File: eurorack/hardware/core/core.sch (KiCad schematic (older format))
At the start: 3 parts, among them U1 STM32F427VGT6, U2 TLV320AIC23BPW, U3 LM1117F-3.3

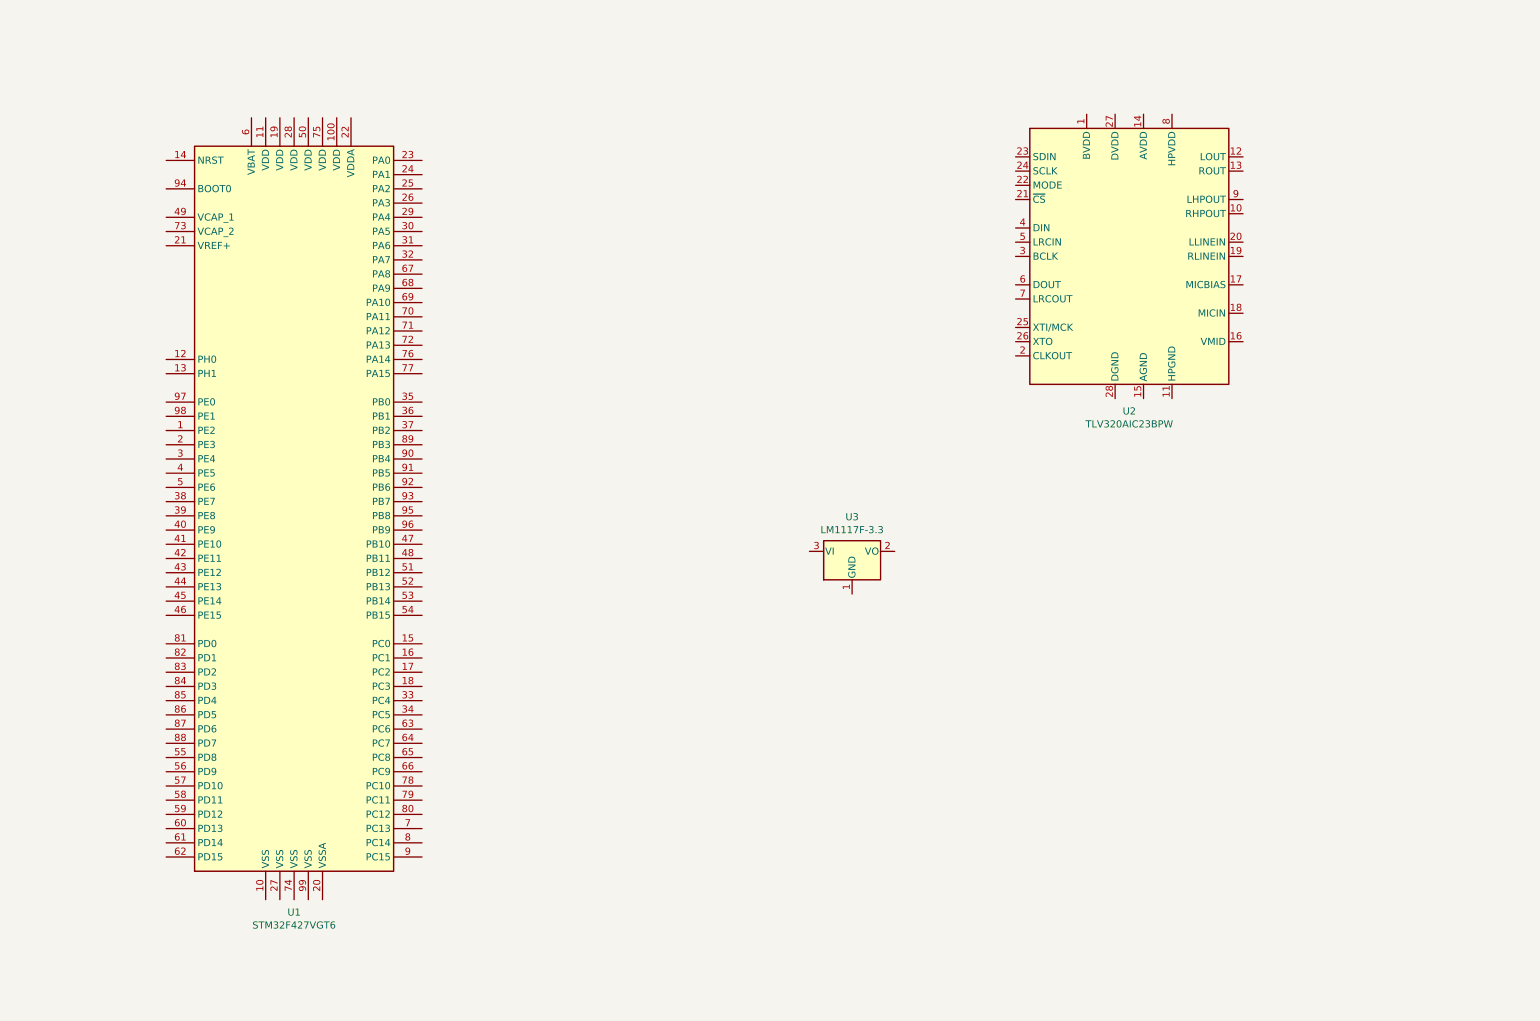
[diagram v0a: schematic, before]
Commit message: Add connections to eurorack core
Signed-off-by: Petr Horacek <hrck@protonmail.com>
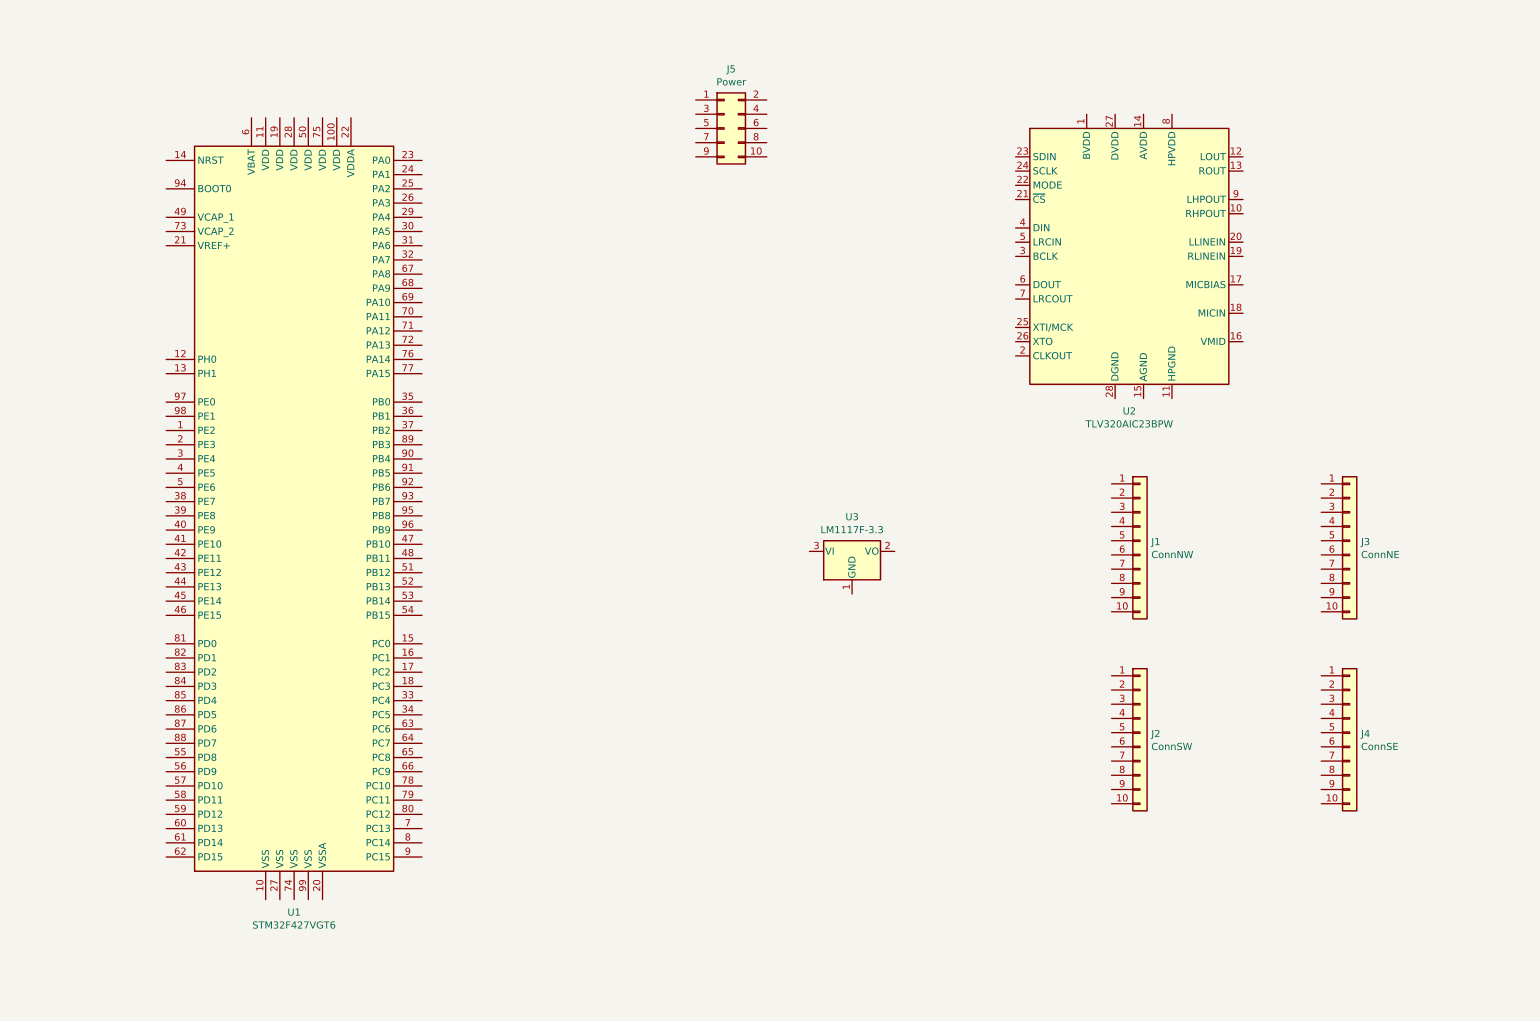
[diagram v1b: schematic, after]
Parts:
- added J1: ConnNW, Connector_PinHeader_2.54mm:PinHeader_1x10_P2.54mm_Vertical, symbol Connector_Generic:Conn_01x10
- added J2: ConnSW, Connector_PinHeader_2.54mm:PinHeader_1x10_P2.54mm_Vertical, symbol Connector_Generic:Conn_01x10
- added J3: ConnNE, Connector_PinHeader_2.54mm:PinHeader_1x10_P2.54mm_Vertical, symbol Connector_Generic:Conn_01x10
- added J4: ConnSE, Connector_PinHeader_2.54mm:PinHeader_1x10_P2.54mm_Vertical, symbol Connector_Generic:Conn_01x10
- added J5: Power, Connector_PinHeader_2.54mm:PinHeader_2x05_P2.54mm_Vertical, symbol Connector_Generic:Conn_02x05_Odd_Even
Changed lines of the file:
@@
+	1    0    0    -1
+$EndComp
+$Comp
+L Connector_Generic:Conn_01x10 J1
+U 1 1 60AE94CD
+P 8425 4300
+F 0 "J1" H 8505 4292 50  0000 L CNN
+F 1 "ConnNW" H 8505 4201 50  0000 L CNN
+F 2 "Connector_PinHeader_2.54mm:PinHeader_1x10_P2.54mm_Vertical" H 8425 4300 50  0001 C CNN
+F 3 "~" H 8425 4300 50  0001 C CNN
+	1    8425 4300
+	1    0    0    -1
+$EndComp
+$Comp
+L Connector_Generic:Conn_01x10 J2
+U 1 1 60AEC1D4
+P 8425 5650
+F 0 "J2" H 8505 5642 50  0000 L CNN
+F 1 "ConnSW" H 8505 5551 50  0000 L CNN
+F 2 "Connector_PinHeader_2.54mm:PinHeader_1x10_P2.54mm_Vertical" H 8425 5650 50  0001 C CNN
+F 3 "~" H 8425 5650 50  0001 C CNN
+	1    8425 5650
+	1    0    0    -1
+$EndComp
+$Comp
+L Connector_Generic:Conn_01x10 J3
+U 1 1 60AED02D
+P 9900 4300
+F 0 "J3" H 9980 4292 50  0000 L CNN
+F 1 "ConnNE" H 9980 4201 50  0000 L CNN
+F 2 "Connector_PinHeader_2.54mm:PinHeader_1x10_P2.54mm_Vertical" H 9900 4300 50  0001 C CNN
+F 3 "~" H 9900 4300 50  0001 C CNN
+	1    9900 4300
+	1    0    0    -1
+$EndComp
+$Comp
+L Connector_Generic:Conn_01x10 J4
+U 1 1 60AED5FD
+P 9900 5650
+F 0 "J4" H 9980 5642 50  0000 L CNN
+F 1 "ConnSE" H 9980 5551 50  0000 L CNN
+F 2 "Connector_PinHeader_2.54mm:PinHeader_1x10_P2.54mm_Vertical" H 9900 5650 50  0001 C CNN
+F 3 "~" H 9900 5650 50  0001 C CNN
+	1    9900 5650
+	1    0    0    -1
+$EndComp
+$Comp
+L Connector_Generic:Conn_02x05_Odd_Even J5
+U 1 1 60AF91AD
+P 5500 1400
+F 0 "J5" H 5550 1817 50  0000 C CNN
+F 1 "Power" H 5550 1726 50  0000 C CNN
+F 2 "Connector_PinHeader_2.54mm:PinHeader_2x05_P2.54mm_Vertical" H 5500 1400 50  0001 C CNN
+F 3 "~" H 5500 1400 50  0001 C CNN
+	1    5500 1400
 	1    0    0    -1
 $EndComp

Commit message: Add basic MCU peripherals and power
Signed-off-by: Petr Horacek <hrck@protonmail.com>
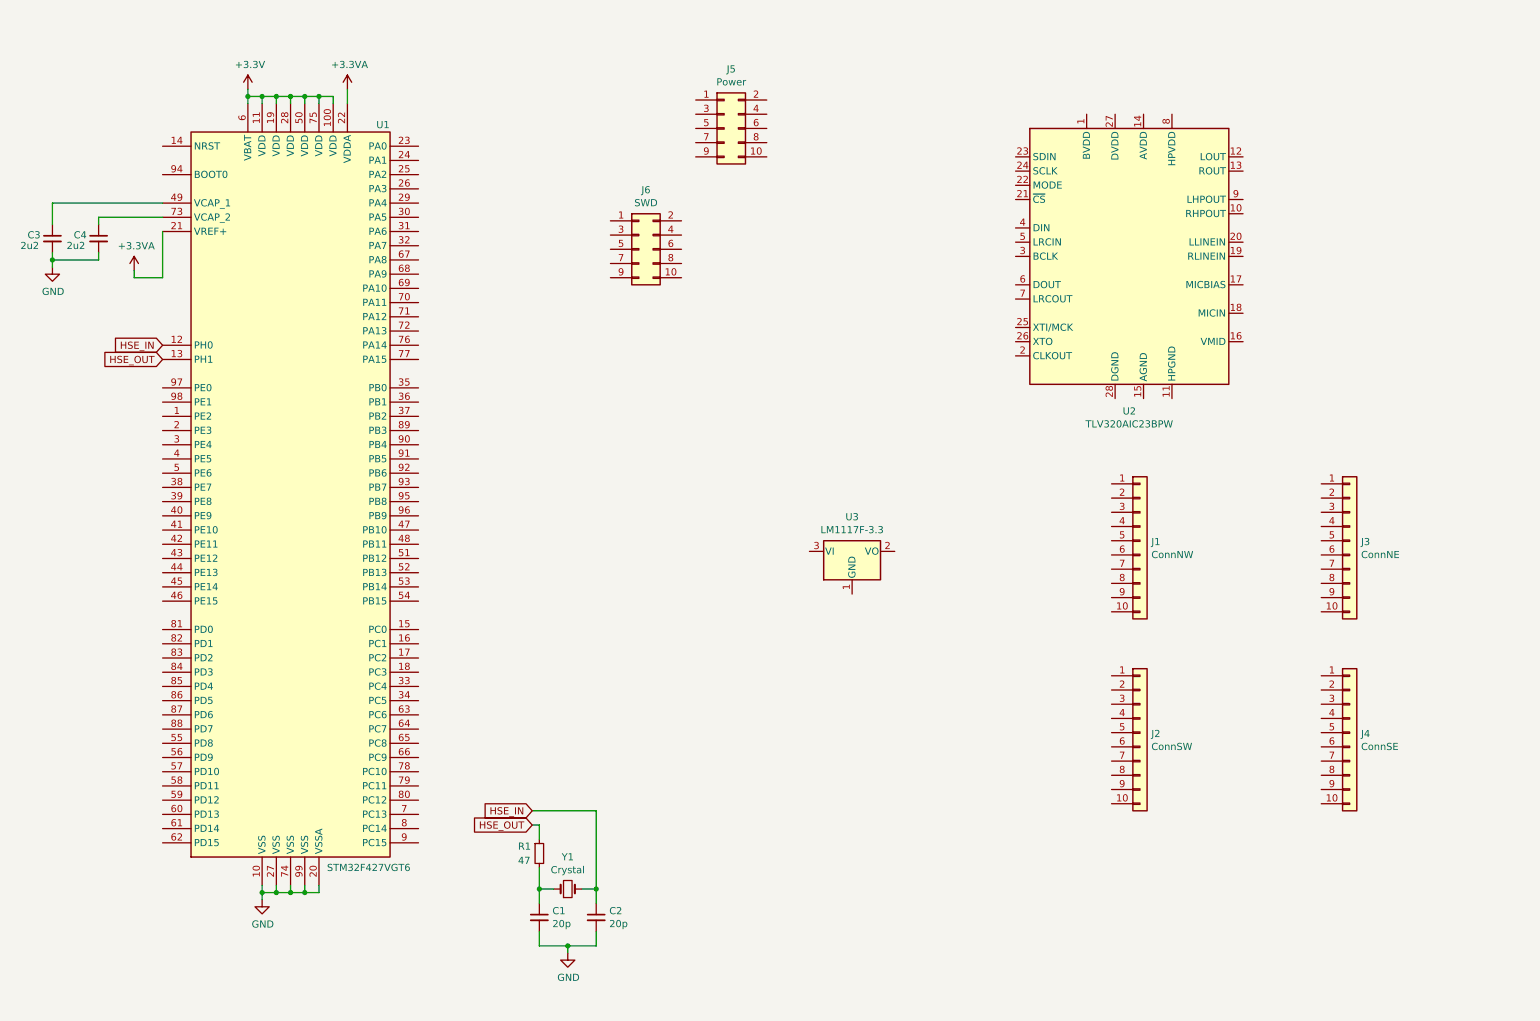
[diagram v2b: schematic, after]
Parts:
- added C1, C2: 20p, Capacitor_SMD:C_0402_1005Metric, symbol Device:C_Small
- added C3, C4: 2u2, Capacitor_SMD:C_0603_1608Metric, symbol Device:C_Small
- added J6: SWD, Connector_PinHeader_2.54mm:PinHeader_2x05_P2.54mm_Vertical, symbol Connector_Generic:Conn_02x05_Odd_Even
- added R1: 47, Resistor_SMD:R_0402_1005Metric, symbol Device:R_Small
- added Y1: Crystal, Crystal:Crystal_SMD_5032-2Pin_5.0x3.2mm, symbol Device:Crystal_Small
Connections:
- net GND: now reaches U1.10 (VSS)
- net GND: now also U1.20 (VSSA), U1.27 (VSS), U1.74 (VSS), U1.99 (VSS), C1.2, C2.2, C3.2, C4.2
- net +3V3: now reaches U1.100 (VDD)
- net +3V3: now also U1.11 (VDD), U1.19 (VDD), U1.28 (VDD), U1.50 (VDD), U1.6 (VBAT), U1.75 (VDD)
- net HSE_IN: now reaches U1.12 (PH0)
- net HSE_IN: now also C2.1, Y1.2
- net HSE_OUT: now reaches U1.13 (PH1)
- net HSE_OUT: now also R1.1
- net +3.3VA: now reaches U1.21 (VREF+)
- net +3.3VA: now also U1.22 (VDDA)
- net at U1.49 (VCAP_1): now also C3.1
- net at U1.73 (VCAP_2): now also C4.1
- new net: C1.1, R1.2, Y1.1
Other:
- moved on the sheet: U1

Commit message: Add reset and boot buttons
Signed-off-by: Petr Horacek <hrck@protonmail.com>
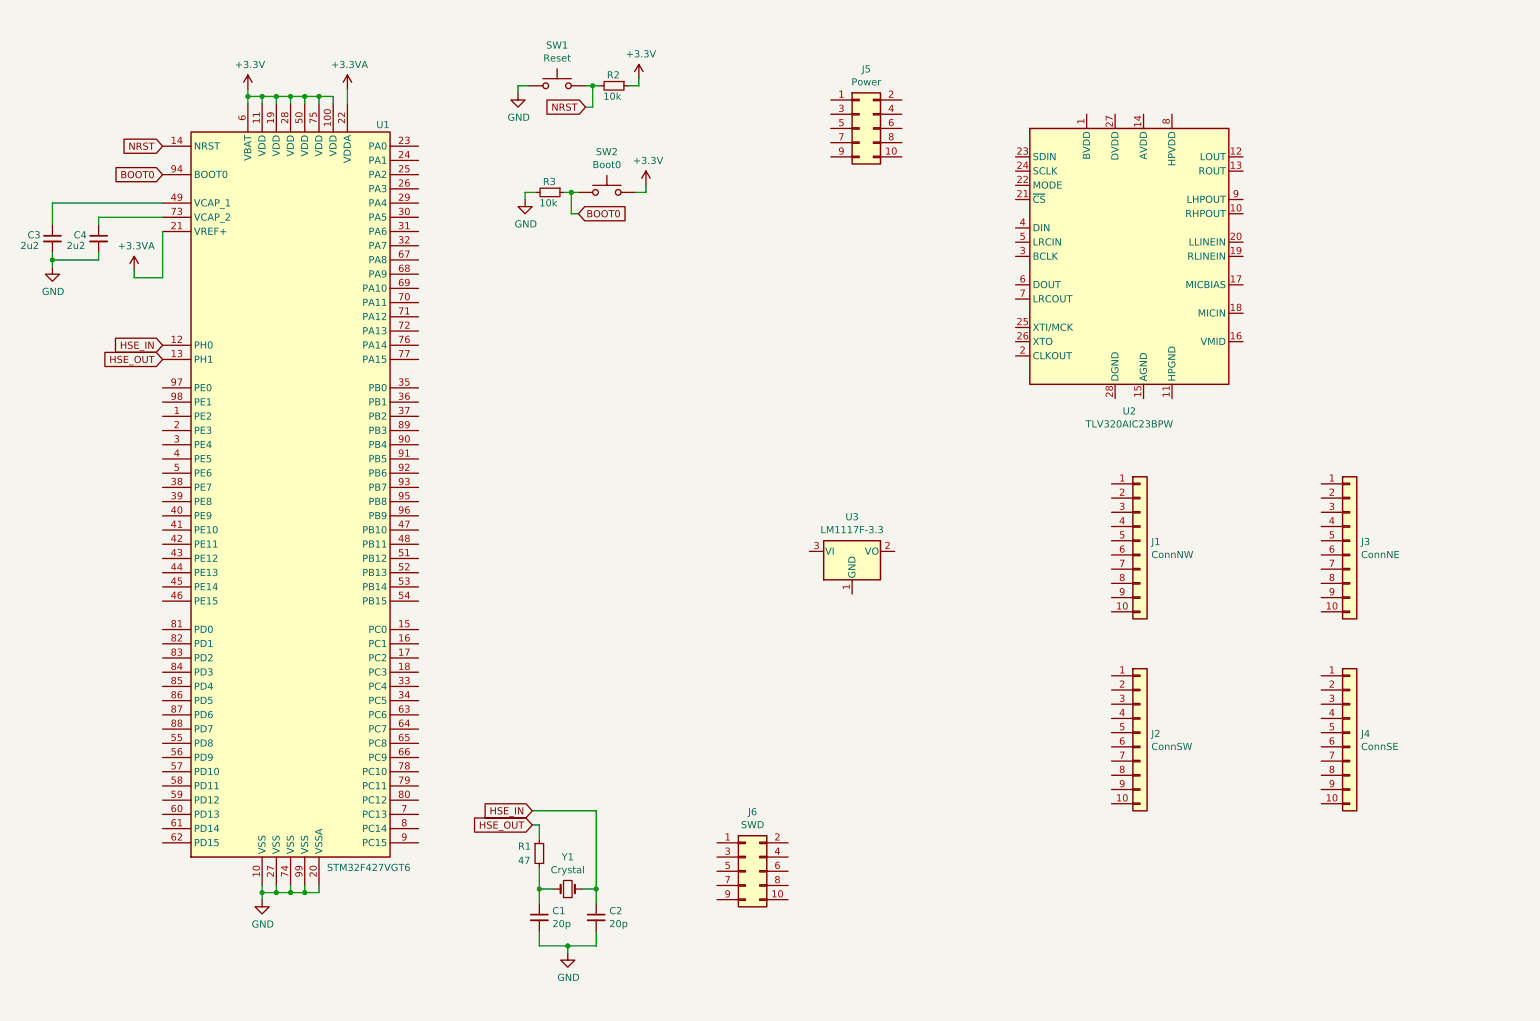
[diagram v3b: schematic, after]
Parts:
- added R2, R3: 10k, Resistor_SMD:R_0402_1005Metric, symbol Device:R_Small
- added SW1: Reset, Button_Switch_SMD:SW_Push_SPST_NO_Alps_SKRK, symbol Switch:SW_Push
- added SW2: Boot0, Button_Switch_SMD:SW_Push_SPST_NO_Alps_SKRK, symbol Switch:SW_Push
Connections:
- net +3V3: now also R2.1, SW2.2
- net GND: now also R3.2, SW1.1
- net NRST: now reaches U1.14 (NRST)
- net NRST: now also R2.2, SW1.2
- net BOOT0: now reaches U1.94 (BOOT0)
- net BOOT0: now also R3.1, SW2.1
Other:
- moved on the sheet: J5, J6
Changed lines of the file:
@@
 L Connector_Generic:Conn_02x05_Odd_Even J5
 U 1 1 60AF91AD
-P 5500 1400
-F 0 "J5" H 5550 1817 50  0000 C CNN
-F 1 "Power" H 5550 1726 50  0000 C CNN
-F 2 "Connector_PinHeader_2.54mm:PinHeader_2x05_P2.54mm_Vertical" H 5500 1400 50  0001 C CNN
-F 3 "~" H 5500 1400 50  0001 C CNN
-	1    5500 1400
+P 6450 1400
+F 0 "J5" H 6500 1817 50  0000 C CNN
+F 1 "Power" H 6500 1726 50  0000 C CNN
+F 2 "Connector_PinHeader_2.54mm:PinHeader_2x05_P2.54mm_Vertical" H 6450 1400 50  0001 C CNN
+F 3 "~" H 6450 1400 50  0001 C CNN
+	1    6450 1400
 	1    0    0    -1
 $EndComp
@@
 L Connector_Generic:Conn_02x05_Odd_Even J6
 U 1 1 60B0973B
-P 4900 2250
-F 0 "J6" H 4950 2667 50  0000 C CNN
-F 1 "SWD" H 4950 2576 50  0000 C CNN
-F 2 "Connector_PinHeader_2.54mm:PinHeader_2x05_P2.54mm_Vertical" H 4900 2250 50  0001 C CNN
-F 3 "~" H 4900 2250 50  0001 C CNN
-	1    4900 2250
+P 5650 6625
+F 0 "J6" H 5700 7042 50  0000 C CNN
+F 1 "SWD" H 5700 6951 50  0000 C CNN
+F 2 "Connector_PinHeader_2.54mm:PinHeader_2x05_P2.54mm_Vertical" H 5650 6625 50  0001 C CNN
+F 3 "~" H 5650 6625 50  0001 C CNN
+	1    5650 6625
 	1    0    0    -1
 $EndComp
@@
 Wire Wire Line
 	2350 6775 2450 6775
+Text GLabel 1550 1525 0    50   Input ~ 0
+NRST
+Text GLabel 1550 1725 0    50   Input ~ 0
+BOOT0
+$Comp
+L Switch:SW_Push SW1
+U 1 1 60BE2DB3
+P 4325 1100
+F 0 "SW1" H 4325 1385 50  0000 C CNN
+F 1 "Reset" H 4325 1294 50  0000 C CNN
+F 2 "Button_Switch_SMD:SW_Push_SPST_NO_Alps_SKRK" H 4325 1300 50  0001 C CNN
+F 3 "~" H 4325 1300 50  0001 C CNN
+	1    4325 1100
+	1    0    0    -1
+$EndComp
+$Comp
+L Device:R_Small R2
+U 1 1 60BE4509
+P 4725 1100
+F 0 "R2" V 4650 1050 50  0000 L CNN
+F 1 "10k" V 4800 1025 50  0000 L CNN
+F 2 "Resistor_SMD:R_0402_1005Metric" H 4725 1100 50  0001 C CNN
+F 3 "~" H 4725 1100 50  0001 C CNN
+	1    4725 1100
+	0    1    1    0
+$EndComp
+$Comp
+L power:GND #PWR05
+U 1 1 60BE9668
+P 4050 1150
+F 0 "#PWR05" H 4050 900 50  0001 C CNN
+F 1 "GND" H 4055 977 50  0000 C CNN
+F 2 "" H 4050 1150 50  0001 C CNN
+F 3 "" H 4050 1150 50  0001 C CNN
+	1    4050 1150
+	1    0    0    -1
+$EndComp
+$Comp
+L power:+3.3V #PWR06
+U 1 1 60BEA09E
+P 4900 1050
+F 0 "#PWR06" H 4900 900 50  0001 C CNN
+F 1 "+3.3V" H 4915 1223 50  0000 C CNN
+F 2 "" H 4900 1050 50  0001 C CNN
+F 3 "" H 4900 1050 50  0001 C CNN
+	1    4900 1050
+	1    0    0    -1
+$EndComp
+Wire Wire Line
+	4825 1100 4900 1100
+Wire Wire Line
+	4900 1100 4900 1050
+Wire Wire Line
+	4125 1100 4050 1100
+Wire Wire Line
+	4050 1100 4050 1150
+$Comp
+L Switch:SW_Push SW2
+U 1 1 60C09AF8
+P 4675 1850
+F 0 "SW2" H 4675 2135 50  0000 C CNN
+F 1 "Boot0" H 4675 2044 50  0000 C CNN
+F 2 "Button_Switch_SMD:SW_Push_SPST_NO_Alps_SKRK" H 4675 2050 50  0001 C CNN
+F 3 "~" H 4675 2050 50  0001 C CNN
+	1    4675 1850
+	1    0    0    -1
+$EndComp
+$Comp
+L Device:R_Small R3
+U 1 1 60C0A50D
+P 4275 1850
+F 0 "R3" V 4200 1800 50  0000 L CNN
+F 1 "10k" V 4350 1775 50  0000 L CNN
+F 2 "Resistor_SMD:R_0402_1005Metric" H 4275 1850 50  0001 C CNN
+F 3 "~" H 4275 1850 50  0001 C CNN
+	1    4275 1850
+	0    1    1    0
+$EndComp
+$Comp
+L power:GND #PWR0103
+U 1 1 60C0C66D
+P 4100 1900
+F 0 "#PWR0103" H 4100 1650 50  0001 C CNN
+F 1 "GND" H 4105 1727 50  0000 C CNN
+F 2 "" H 4100 1900 50  0001 C CNN
+F 3 "" H 4100 1900 50  0001 C CNN
+	1    4100 1900
+	1    0    0    -1
+$EndComp
+Wire Wire Line
+	4175 1850 4100 1850
+Wire Wire Line
+	4100 1850 4100 1900
+$Comp
+L power:+3.3V #PWR0104
+U 1 1 60C0E060
+P 4950 1800
+F 0 "#PWR0104" H 4950 1650 50  0001 C CNN
+F 1 "+3.3V" H 4965 1973 50  0000 C CNN
+F 2 "" H 4950 1800 50  0001 C CNN
+F 3 "" H 4950 1800 50  0001 C CNN
+	1    4950 1800
+	1    0    0    -1
+$EndComp
+Wire Wire Line
+	4875 1850 4950 1850
+Wire Wire Line
+	4950 1850 4950 1800
+Wire Wire Line
+	4525 1100 4575 1100
+Text GLabel 4525 1250 0    50   Input ~ 0
+NRST
+Wire Wire Line
+	4525 1250 4575 1250
+Wire Wire Line
+	4575 1250 4575 1100
+Connection ~ 4575 1100
+Wire Wire Line
+	4575 1100 4625 1100
+Wire Wire Line
+	4375 1850 4425 1850
+Text GLabel 4475 2000 2    50   Input ~ 0
+BOOT0
+Wire Wire Line
+	4475 2000 4425 2000
+Wire Wire Line
+	4425 2000 4425 1850
+Connection ~ 4425 1850
+Wire Wire Line
+	4425 1850 4475 1850
 $EndSCHEMATC
